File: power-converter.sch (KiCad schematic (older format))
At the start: 18 parts

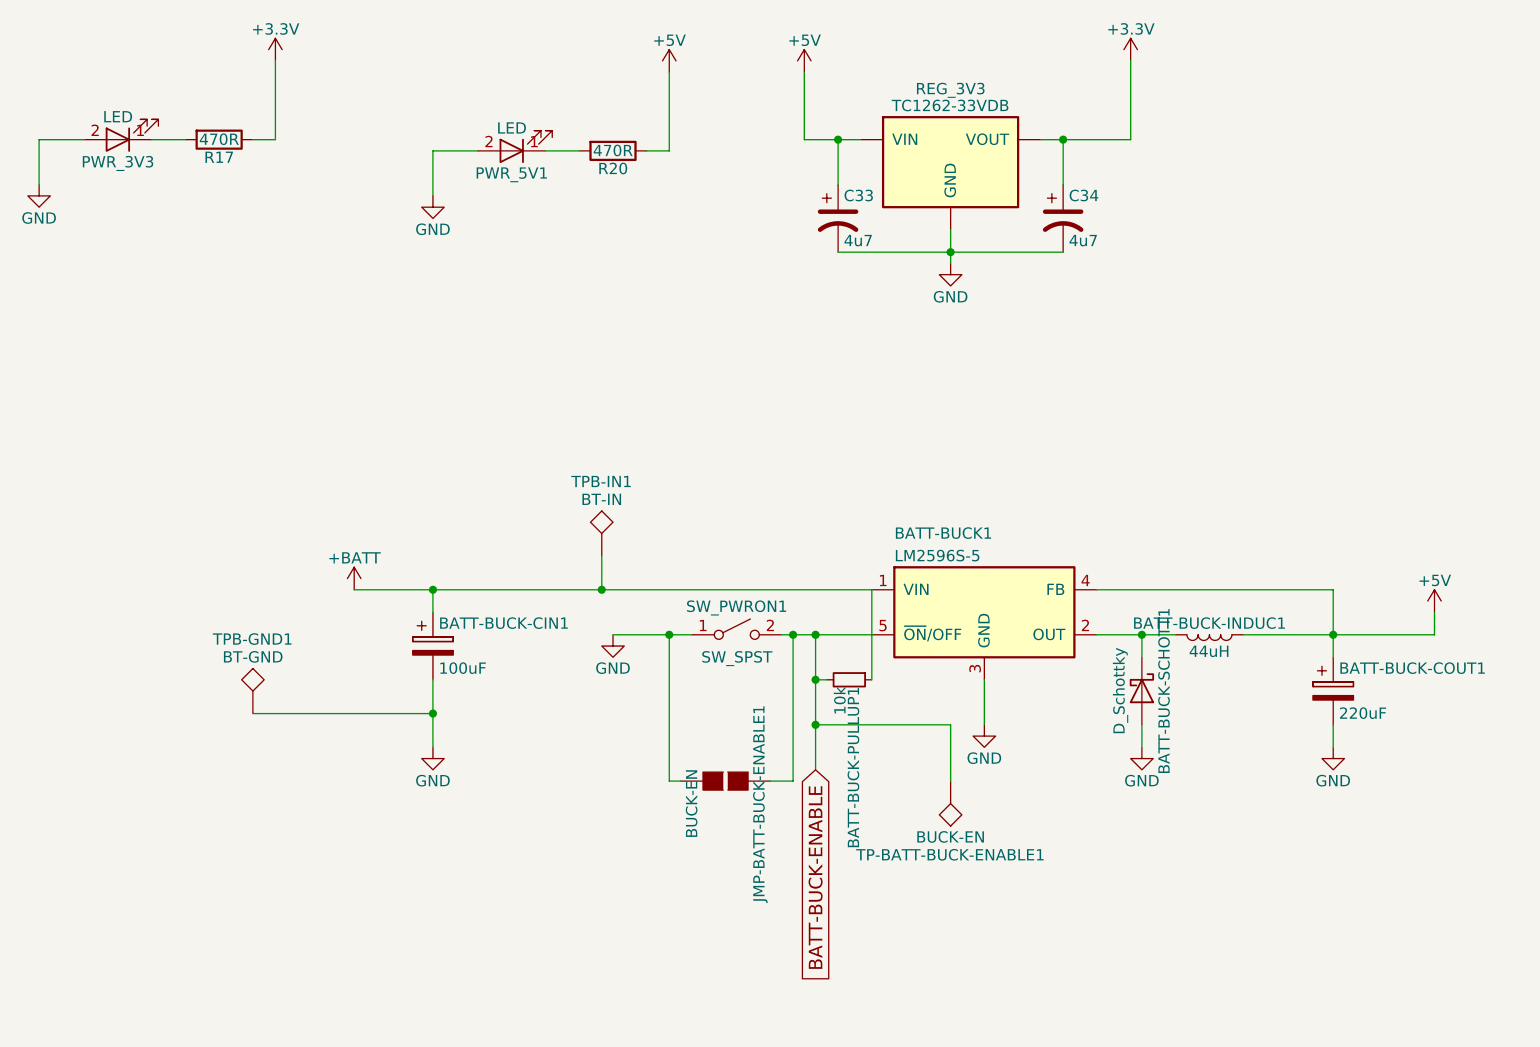
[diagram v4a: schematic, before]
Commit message: Name changes on silk
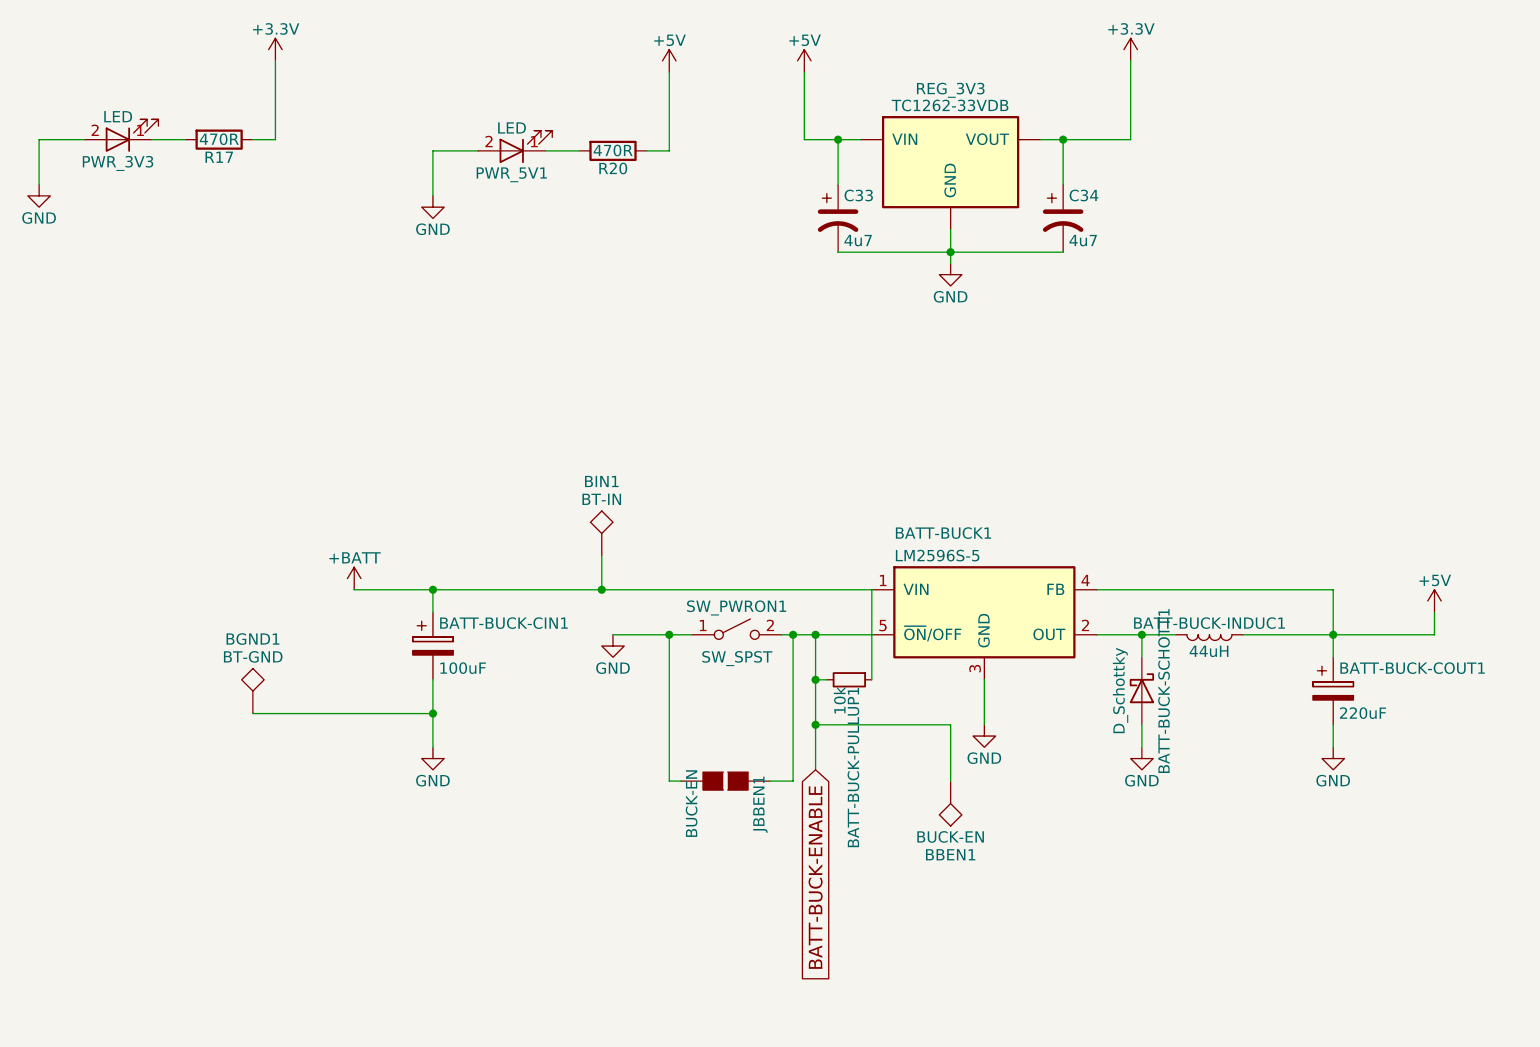
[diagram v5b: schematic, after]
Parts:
- SW_PWRON1: footprint Buttons_Switches_SMD:SW_SPST_EVQQ2 -> Buttons_Switches_SMD:SW_SPST_EVQPE1
- renumbered TP-BATT-BUCK-ENABLE1 to BBEN1, TPB-GND1 to BGND1, TPB-IN1 to BIN1, JMP-BATT-BUCK-ENABLE1 to JBBEN1
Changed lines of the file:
@@
 F 0 "SW_PWRON1" H 5550 4025 50  0000 C CNN
 F 1 "SW_SPST" H 5550 3800 50  0000 C CNN
-F 2 "Buttons_Switches_SMD:SW_SPST_EVQQ2" H 5550 3900 50  0001 C CNN
+F 2 "Buttons_Switches_SMD:SW_SPST_EVQPE1" H 5550 3900 50  0001 C CNN
 F 3 "" H 5550 3900 50  0001 C CNN
 	1    5550 3900
@@
 	5750 3900 6150 3900
 $Comp
-L GND #PWR28
+L GND #PWR023
 U 1 1 5B2D2C35
 P 5000 3900
-F 0 "#PWR28" H 5000 3650 50  0001 C CNN
+F 0 "#PWR023" H 5000 3650 50  0001 C CNN
 F 1 "GND" H 5000 3750 50  0000 C CNN
 F 2 "" H 5000 3900 50  0001 C CNN
@@
 Connection ~ 8200 3900
 $Comp
-L GND #PWR34
+L GND #PWR024
 U 1 1 5B2D2C55
 P 7350 4400
-F 0 "#PWR34" H 7350 4150 50  0001 C CNN
+F 0 "#PWR024" H 7350 4150 50  0001 C CNN
 F 1 "GND" H 7350 4250 50  0000 C CNN
 F 2 "" H 7350 4400 50  0001 C CNN
@@
 $EndComp
 $Comp
-L GND #PWR35
+L GND #PWR025
 U 1 1 5B2D2C63
 P 8200 4400
-F 0 "#PWR35" H 8200 4150 50  0001 C CNN
+F 0 "#PWR025" H 8200 4150 50  0001 C CNN
 F 1 "GND" H 8200 4250 50  0000 C CNN
 F 2 "" H 8200 4400 50  0001 C CNN
@@
 	8200 4300 8200 4400
 $Comp
-L GND #PWR32
+L GND #PWR026
 U 1 1 5B2D2C6A
 P 6650 4300
-F 0 "#PWR32" H 6650 4050 50  0001 C CNN
+F 0 "#PWR026" H 6650 4050 50  0001 C CNN
 F 1 "GND" H 6650 4150 50  0000 C CNN
 F 2 "" H 6650 4300 50  0001 C CNN
@@
 	3850 3700 6150 3700
 $Comp
-L GND #PWR27
+L GND #PWR027
 U 1 1 5B2D2C79
 P 4200 4400
-F 0 "#PWR27" H 4200 4150 50  0001 C CNN
+F 0 "#PWR027" H 4200 4150 50  0001 C CNN
 F 1 "GND" H 4200 4250 50  0000 C CNN
 F 2 "" H 4200 4400 50  0001 C CNN
@@
 Connection ~ 5900 4300
 $Comp
-L GS2 JMP-BATT-BUCK-ENABLE1
+L GS2 JBBEN1
 U 1 1 5B2D2C8C
 P 5500 4550
-F 0 "JMP-BATT-BUCK-ENABLE1" H 5600 4700 50  0000 C CNN
+F 0 "JBBEN1" H 5600 4700 50  0000 C CNN
 F 1 "BUCK-EN" H 5600 4401 50  0000 C CNN
 F 2 "Connect:GS2" V 5574 4550 50  0001 C CNN
@@
 Connection ~ 5800 3900
 $Comp
-L TEST TP-BATT-BUCK-ENABLE1
+L TEST BBEN1
 U 1 1 5B2D2C9C
 P 6500 4550
-F 0 "TP-BATT-BUCK-ENABLE1" H 6500 4850 50  0000 C BNN
+F 0 "BBEN1" H 6500 4850 50  0000 C BNN
 F 1 "BUCK-EN" H 6500 4800 50  0000 C CNN
 F 2 "Measurement_Points:Measurement_Point_Round-SMD-Pad_Small" H 6500 4550 50  0001 C CNN
@@
 	6500 4300 6500 4550
 $Comp
-L +BATT #PWR25
+L +BATT #PWR028
 U 1 1 5B2D2CA5
 P 3850 3700
-F 0 "#PWR25" H 3850 3550 50  0001 C CNN
+F 0 "#PWR028" H 3850 3550 50  0001 C CNN
 F 1 "+BATT" H 3850 3840 50  0000 C CNN
 F 2 "" H 3850 3700 50  0001 C CNN
@@
 Connection ~ 4200 3700
 $Comp
-L TEST TPB-IN1
+L TEST BIN1
 U 1 1 5B2D2CAC
 P 4950 3550
-F 0 "TPB-IN1" H 4950 3850 50  0000 C BNN
+F 0 "BIN1" H 4950 3850 50  0000 C BNN
 F 1 "BT-IN" H 4950 3800 50  0000 C CNN
 F 2 "Measurement_Points:Measurement_Point_Round-SMD-Pad_Small" H 4950 3550 50  0001 C CNN
@@
 Connection ~ 4950 3700
 $Comp
-L TEST TPB-GND1
+L TEST BGND1
 U 1 1 5B2D2CB5
 P 3400 4250
-F 0 "TPB-GND1" H 3400 4550 50  0000 C BNN
+F 0 "BGND1" H 3400 4550 50  0000 C BNN
 F 1 "BT-GND" H 3400 4500 50  0000 C CNN
 F 2 "Measurement_Points:Measurement_Point_Round-SMD-Pad_Small" H 3400 4250 50  0001 C CNN
@@
 Connection ~ 4200 4250
 $Comp
-L +3.3V #PWR24
+L +3.3V #PWR029
 U 1 1 5B2DAE29
 P 3500 1350
-F 0 "#PWR24" H 3500 1200 50  0001 C CNN
+F 0 "#PWR029" H 3500 1200 50  0001 C CNN
 F 1 "+3.3V" H 3500 1490 50  0000 C CNN
 F 2 "" H 3500 1350 50  0001 C CNN
@@
 $EndComp
 $Comp
-L +3.3V #PWR33
+L +3.3V #PWR030
 U 1 1 5B2DAE36
 P 7300 1350
-F 0 "#PWR33" H 7300 1200 50  0001 C CNN
+F 0 "#PWR030" H 7300 1200 50  0001 C CNN
 F 1 "+3.3V" H 7300 1490 50  0000 C CNN
 F 2 "" H 7300 1350 50  0001 C CNN
@@
 $EndComp
 $Comp
-L GND #PWR31
+L GND #PWR031
 U 1 1 5B2DAE42
 P 6500 2250
-F 0 "#PWR31" H 6500 2000 50  0001 C CNN
+F 0 "#PWR031" H 6500 2000 50  0001 C CNN
 F 1 "GND" H 6500 2100 50  0000 C CNN
 F 2 "" H 6500 2250 50  0001 C CNN
@@
 $EndComp
 $Comp
-L GND #PWR23
+L GND #PWR032
 U 1 1 5B2DAE4F
 P 2450 1900
-F 0 "#PWR23" H 2450 1650 50  0001 C CNN
+F 0 "#PWR032" H 2450 1650 50  0001 C CNN
 F 1 "GND" H 2450 1750 50  0000 C CNN
 F 2 "" H 2450 1900 50  0001 C CNN
@@
 $EndComp
 $Comp
-L +5V #PWR36
+L +5V #PWR033
 U 1 1 5B114C95
 P 8650 3800
-F 0 "#PWR36" H 8650 3650 50  0001 C CNN
+F 0 "#PWR033" H 8650 3650 50  0001 C CNN
 F 1 "+5V" H 8650 3940 50  0000 C CNN
 F 2 "" H 8650 3800 50  0001 C CNN
@@
 	8650 3900 8650 3800
 $Comp
-L +5V #PWR30
+L +5V #PWR034
 U 1 1 5B115086
 P 5850 1400
-F 0 "#PWR30" H 5850 1250 50  0001 C CNN
+F 0 "#PWR034" H 5850 1250 50  0001 C CNN
 F 1 "+5V" H 5850 1540 50  0000 C CNN
 F 2 "" H 5850 1400 50  0001 C CNN
@@
 $EndComp
 $Comp
-L GND #PWR26
+L GND #PWR035
 U 1 1 5B16EE02
 P 4200 1950
-F 0 "#PWR26" H 4200 1700 50  0001 C CNN
+F 0 "#PWR035" H 4200 1700 50  0001 C CNN
 F 1 "GND" H 4200 1800 50  0000 C CNN
 F 2 "" H 4200 1950 50  0001 C CNN
@@
 	5250 1750 5250 1400
 $Comp
-L +5V #PWR29
+L +5V #PWR036
 U 1 1 5B18DEB1
 P 5250 1400
-F 0 "#PWR29" H 5250 1250 50  0001 C CNN
+F 0 "#PWR036" H 5250 1250 50  0001 C CNN
 F 1 "+5V" H 5250 1540 50  0000 C CNN
 F 2 "" H 5250 1400 50  0001 C CNN
